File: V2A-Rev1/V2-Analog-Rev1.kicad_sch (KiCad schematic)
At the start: 39 parts, among them J1 Apple II, J2 DB15_Female_HighDensity_Mount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, J3 NOPAL, J4 NOWIFI, J5 VGA, J6 VGA, U1 SN74LVC8T245DGVR, U2 SN74LVC8T245DGVR, U3 SN74LVC8T245DGVR, U4 SN74LVC8T245DGVR, U5 PALCE16V8H-5JC/5, U6 Pi PICO W, U7 AZ1117I-H-3.3

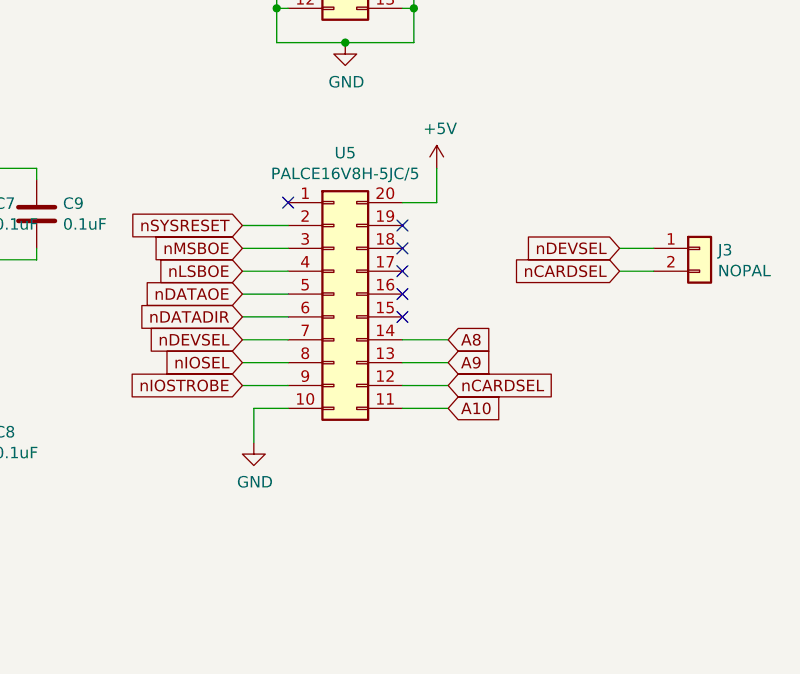
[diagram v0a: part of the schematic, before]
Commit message: Update design to use a PLCC socket for PAL/GAL.
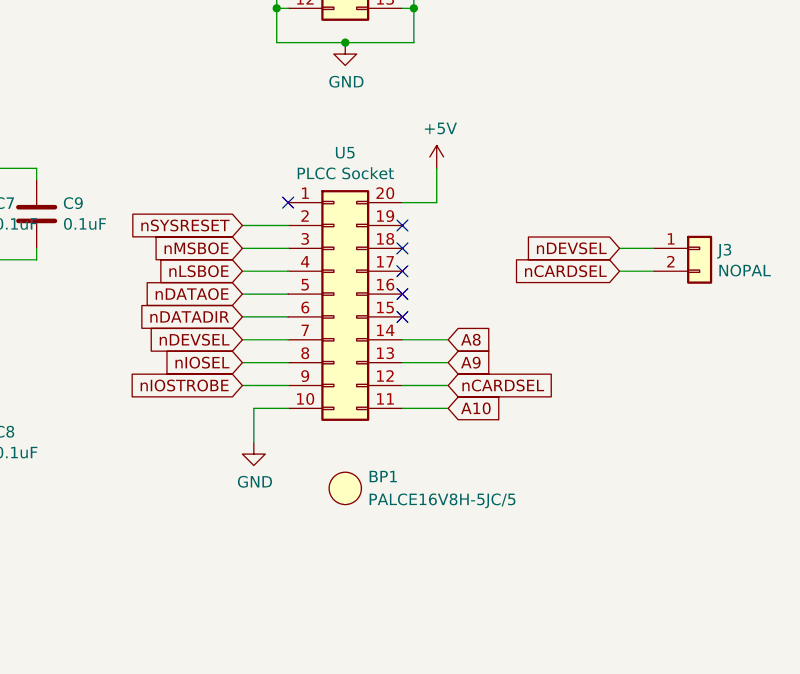
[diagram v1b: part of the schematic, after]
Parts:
- added BP1: PALCE16V8H-5JC/5, V2-Analog-Rev1:BOM_Placeholder, symbol V2-Analog-Rev1:BOM_Placeholder
- U5: value PALCE16V8H-5JC/5 -> PLCC Socket; footprint Package_LCC:PLCC-20 -> Package_LCC:PLCC-20_SMD-Socket; Digi-Key_PN 2156-PALCE16V8H-5JC/5-ND -> AE11102-ND; LCSC C3292615 -> C7058802; MPN PALCE16V8H-5JC/5 -> A-CCS 020-Z-SM; Manufacturer Lattice Semiconductor Corporation -> Assmann WSW Components
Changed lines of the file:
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@@
     (in_bom yes) (on_board yes)
     (property "Reference" "U5" (id 0) (at 234.95 121.4882 0))
-    (property "Value" "PALCE16V8H-5JC/5" (id 1) (at 234.95 123.7996 0))
-    (property "Footprint" "Package_LCC:PLCC-20" (id 2) (at 233.68 137.16 0)
-      (effects (font (size 1.27 1.27)) hide)
-    )
-    (property "Datasheet" "https://rocelec.widen.net/view/pdf/pmuxehviwj/LATTS01075-1.pdf?t.download=true&u=5oefqw" (id 3) (at 233.68 137.16 0)
-      (effects (font (size 1.27 1.27)) hide)
-    )
-    (property "Description" "EE PLD, 5NS, PAL-TYPE" (id 4) (at 233.68 137.16 0)
-      (effects (font (size 1.27 1.27)) hide)
-    )
-    (property "Digi-Key_PN" "2156-PALCE16V8H-5JC/5-ND" (id 5) (at 233.68 137.16 0)
-      (effects (font (size 1.27 1.27)) hide)
-    )
-    (property "MPN" "PALCE16V8H-5JC/5" (id 6) (at 233.68 137.16 0)
-      (effects (font (size 1.27 1.27)) hide)
-    )
-    (property "Manufacturer" "Lattice Semiconductor Corporation" (id 7) (at 233.68 137.16 0)
-      (effects (font (size 1.27 1.27)) hide)
-    )
-    (property "LCSC" "C3292615" (id 8) (at 233.68 137.16 0)
+    (property "Value" "PLCC Socket" (id 1) (at 234.95 123.7996 0))
+    (property "Footprint" "Package_LCC:PLCC-20_SMD-Socket" (id 2) (at 233.68 137.16 0)
+      (effects (font (size 1.27 1.27)) hide)
+    )
+    (property "Datasheet" "http://www.assmann-wsw.com/uploads/datasheets/ASS_0142_CO.pdf" (id 3) (at 233.68 137.16 0)
+      (effects (font (size 1.27 1.27)) hide)
+    )
+    (property "Description" "CONN SOCKET PLCC 20POS TIN" (id 4) (at 233.68 137.16 0)
+      (effects (font (size 1.27 1.27)) hide)
+    )
+    (property "Digi-Key_PN" "AE11102-ND" (id 5) (at 233.68 137.16 0)
+      (effects (font (size 1.27 1.27)) hide)
+    )
+    (property "MPN" "A-CCS 020-Z-SM" (id 6) (at 233.68 137.16 0)
+      (effects (font (size 1.27 1.27)) hide)
+    )
+    (property "Manufacturer" "Assmann WSW Components" (id 7) (at 233.68 137.16 0)
+      (effects (font (size 1.27 1.27)) hide)
+    )
+    (property "LCSC" "C7058802" (id 8) (at 233.68 137.16 0)
       (effects (font (size 1.27 1.27)) hide)
     )
@@
     (pin "2")
   )
+  (symbol (lib_id "V2-Analog-Rev1:BOM_Placeholder") (at 234.95 158.75 0) (unit 1)
+    (in_bom yes) (on_board yes) (fields_autoplaced)
+    (property "Reference" "BP1" (id 0) (at 237.49 157.4799 0)
+      (effects (font (size 1.27 1.27)) (justify left))
+    )
+    (property "Value" "PALCE16V8H-5JC/5" (id 1) (at 237.49 160.0199 0)
+      (effects (font (size 1.27 1.27)) (justify left))
+    )
+    (property "Footprint" "V2-Analog-Rev1:BOM_Placeholder" (id 2) (at 234.95 158.75 0)
+      (effects (font (size 1.27 1.27)) hide)
+    )
+    (property "Datasheet" "~" (id 3) (at 234.95 158.75 0)
+      (effects (font (size 1.27 1.27)) hide)
+    )
+    (property "Description" "EE PLD, 5NS, PAL-TYPE" (id 4) (at 234.95 158.75 0)
+      (effects (font (size 1.27 1.27)) hide)
+    )
+    (property "Digi-Key_PN" "2156-PALCE16V8H-5JC/5-ND" (id 5) (at 234.95 158.75 0)
+      (effects (font (size 1.27 1.27)) hide)
+    )
+    (property "LCSC" "C3292615" (id 6) (at 234.95 158.75 0)
+      (effects (font (size 1.27 1.27)) hide)
+    )
+    (property "MPN" "PALCE16V8H-5JC/5" (id 7) (at 234.95 158.75 0)
+      (effects (font (size 1.27 1.27)) hide)
+    )
+    (property "Manufacturer" "Lattice Semiconductor Corporation" (id 8) (at 234.95 158.75 0)
+      (effects (font (size 1.27 1.27)) hide)
+    )
+  )
   (symbol (lib_id "Connector_Generic:Conn_02x08_Odd_Even") (at 140.97 163.83 180) (unit 1)
     (in_bom yes) (on_board yes) (fields_autoplaced)
@@
       (reference "#PWR0109") (unit 1) (value "GND") (footprint "")
     )
+    (path "/0fb6992d-b8f1-4eb5-800c-0c88afa8e4e5"
+      (reference "BP1") (unit 1) (value "PALCE16V8H-5JC/5") (footprint "V2-Analog-Rev1:BOM_Placeholder")
+    )
     (path "/00000000-0000-0000-0000-00006382c831"
       (reference "C1") (unit 1) (value "0.1uF") (footprint "Capacitor_SMD:C_0402_1005Metric_Pad0.74x0.62mm_HandSolder")
@@
     )
     (path "/00000000-0000-0000-0000-000066540aaf"
-      (reference "U5") (unit 1) (value "PALCE16V8H-5JC/5") (footprint "Package_LCC:PLCC-20")
+      (reference "U5") (unit 1) (value "PLCC Socket") (footprint "Package_LCC:PLCC-20_SMD-Socket")
     )
     (path "/00000000-0000-0000-0000-000063a68952"

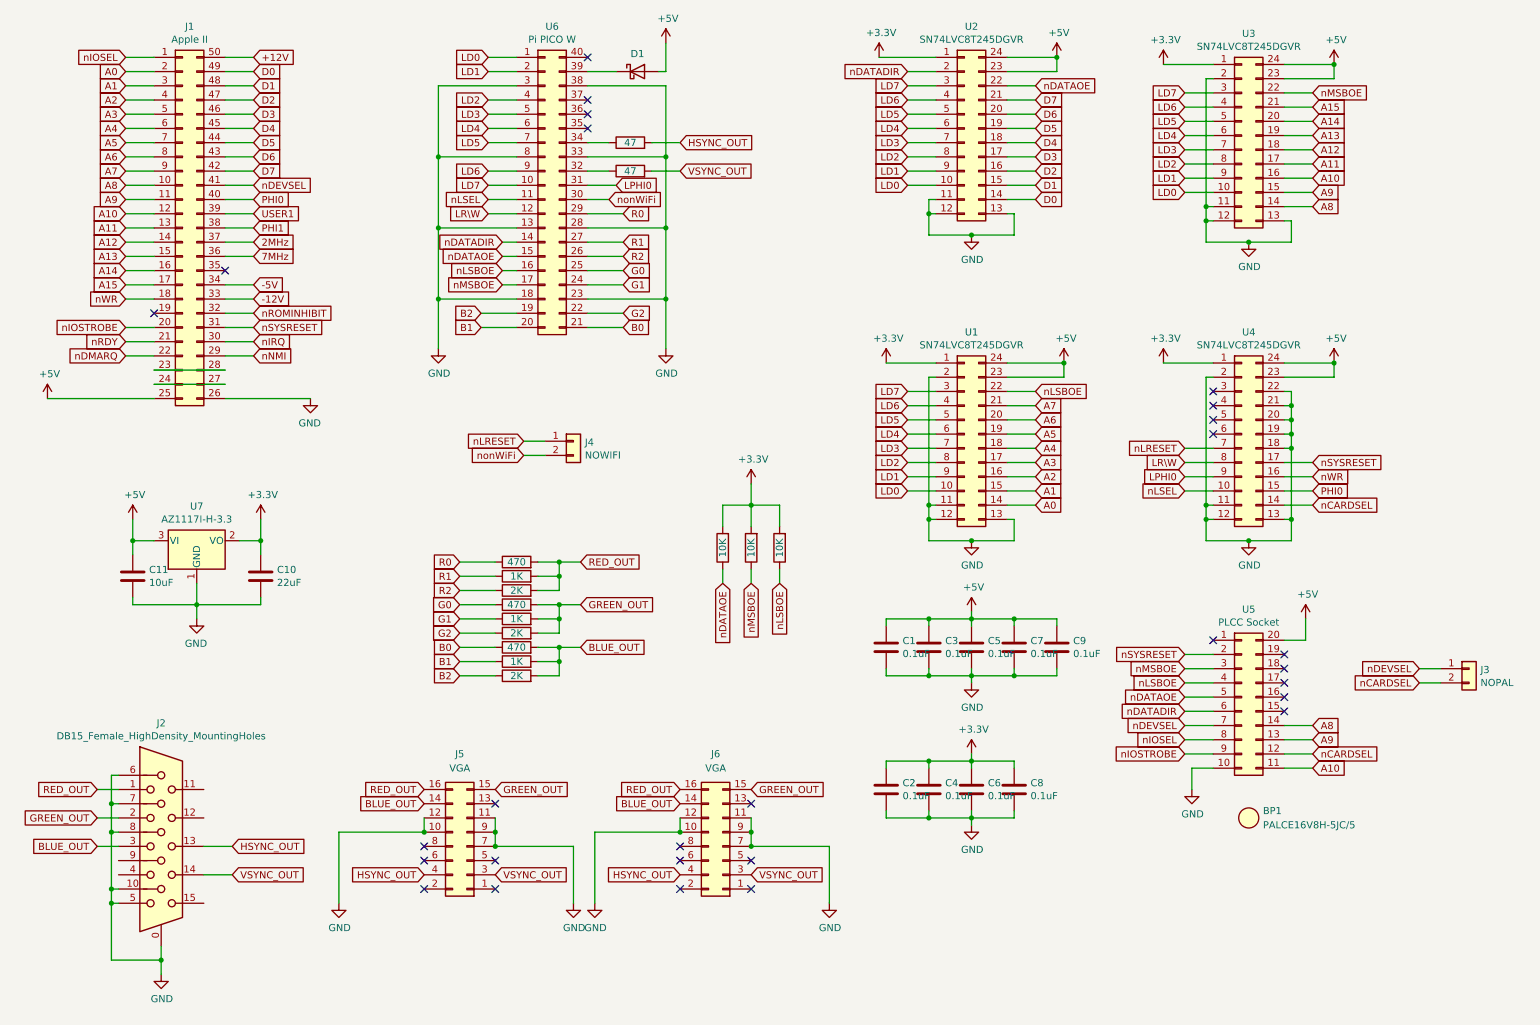
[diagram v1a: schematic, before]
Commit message: Added socket for PLCC. Reorganized layout for improved VGA picture clarity.
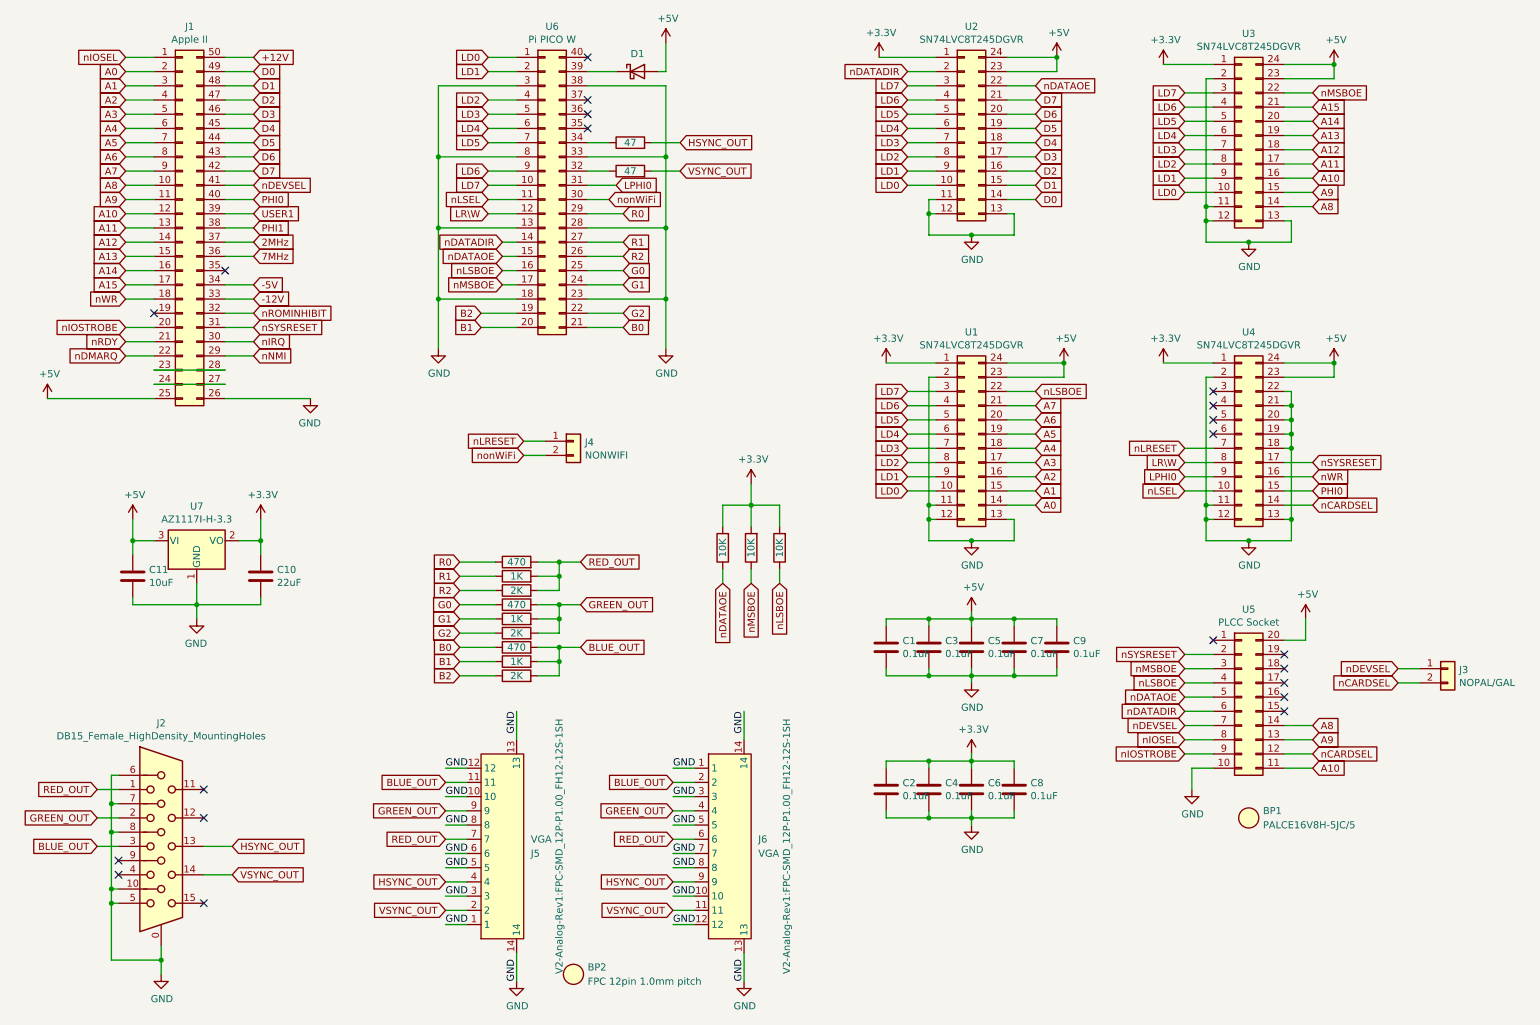
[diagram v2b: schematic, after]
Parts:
- added BP2: FPC 12pin 1.0mm pitch, V2-Analog-Rev1:BOM_Placeholder, symbol V2-Analog-Rev1:BOM_Placeholder
- BP1: Digi-Key_PN 2156-PALCE16V8H-5JC/5-ND -> (none); PN_DigiKey (none) -> 2156-PALCE16V8H-5JC/5-ND; PN_Mouser (none) -> Not Assigned
- C1, C2, C3, C4, C5, C6, C7, C8, C9: Digi-Key_PN 1276-6720-1-ND -> (none); PN_DigiKey (none) -> 1276-6720-1-ND; PN_Mouser (none) -> 187-CL05B104KA5NNNC
- C10: Digi-Key_PN 1276-CL21A226MAYNNNECT-ND -> (none); PN_DigiKey (none) -> 1276-CL21A226MAYNNNECT-ND; PN_Mouser (none) -> 187-CL21A226MAYNNNE
- C11: Digi-Key_PN 1276-2891-1-ND -> (none); PN_DigiKey (none) -> 1276-2891-1-ND; PN_Mouser (none) -> 187-CL21A106KAYNNNE
- D1: Digi-Key_PN 3372-SS14FTR-ND -> (none); PN_DigiKey (none) -> 3372-SS14FTR-ND; PN_Mouser (none) -> 833-SS14FL-TP
- J2: footprint Connector_Dsub:DSUB-15-HD_Female_Horizontal_P2.29x1.98mm_EdgePinOffset3.03mm_Housed_MountingHolesOffset4.94mm -> V2-Analog-Rev1:DSUB-15-HD_Female_Horizontal_P2.29x1.98mm_EdgePinOffset3.03mm_Housed_MountingHolesOffset4.94mm; symbol Connector:DB15_Female_HighDensity_MountingHoles -> V2-Analog-Rev1:DB15_Female_HighDensity_MountingHoles; Digi-Key_PN L77HDE15SD1CH4FVGA-ND -> (none); PN_DigiKey (none) -> L77HDE15SD1CH4FVGA-ND; PN_Mouser (none) -> 523-7HDE15SD1CH4FVGA
- J3: value NOPAL -> NOPAL/GAL
- J4: value NOWIFI -> NONWIFI
- J5, J6: footprint Connector_PinHeader_2.54mm:PinHeader_2x08_P2.54mm_Vertical -> V2-Analog-Rev1:FPC-SMD_12P-P1.00_FH12-12S-1SH; symbol Connector_Generic:Conn_02x08_Odd_Even -> V2-Analog-Rev1:FH12-12S-1SH(55); Digi-Key_PN SAM1058-08-ND -> (none); LCSC C706898 -> C5148307; MPN TSW-108-14-T-D -> FH12-12S-1SH(55); Manufacturer Samtec Inc. -> Hirose Electric Co Ltd; PN_DigiKey (none) -> H124709CT-ND; PN_Mouser (none) -> 798-FH1212S1SH55
- R1, R4, R7: Digi-Key_PN P470LCT-ND -> (none); PN_DigiKey (none) -> P470LCT-ND; PN_Mouser (none) -> 667-ERJ-2RKF4700X
- R10, R11: Digi-Key_PN P47.0LCT-ND -> (none); PN_DigiKey (none) -> P47.0LCT-ND; PN_Mouser (none) -> 667-ERJ-2RKF47R0X
- R12, R13, R14: Digi-Key_PN P10.0KHCT-ND -> (none); PN_DigiKey (none) -> P10.0KHCT-ND; PN_Mouser (none) -> 667-ERJ-3EKF1002V
- R2, R5, R8: Digi-Key_PN P1.00KLCT-ND -> (none); PN_DigiKey (none) -> P1.00KLCT-ND; PN_Mouser (none) -> 667-ERJ-2RKF1001X
- R3, R6, R9: Digi-Key_PN P2.00KLCT-ND -> (none); PN_DigiKey (none) -> P2.00KLCT-ND; PN_Mouser (none) -> 667-ERJ-2RKF2001X
- U1, U2, U3, U4: Digi-Key_PN 296-19287-1-ND -> (none); PN_DigiKey (none) -> 296-19287-1-ND; PN_Mouser (none) -> 595-SN74LVC8T245DGVR
- U5: footprint Package_LCC:PLCC-20_SMD-Socket -> V2-Analog-Rev1:A-CCS_020-Z-SM_SMD-Socket; Digi-Key_PN AE11102-ND -> (none); PN_DigiKey (none) -> AE11102-ND; PN_Mouser (none) -> 517-8420-21B1-RK-TR
- U6: Digi-Key_PN 2648-SC0918CT-ND -> (none); PN_DigiKey (none) -> 2648-SC0918CT-ND; PN_Mouser (none) -> 358-SC0918
- U7: Digi-Key_PN 31-AZ1117H-3.3TRG1CT-ND -> (none); PN_DigiKey (none) -> 31-AZ1117H-3.3TRG1CT-ND; PN_Mouser (none) -> 621-AZ1117H-3.3TRG1
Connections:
- net BLUE_OUT: now also J5.11, J6.2; no longer J5.14 (Pin_14), J6.14 (Pin_14)
- net GND: now also J5.1, J5.13, J5.14, J5.3, J5.5, J5.6, J5.8, J6.1, J6.13, J6.14, J6.3, J6.5, J6.8; no longer J5.11 (Pin_11), J5.7 (Pin_7), J5.9 (Pin_9), J6.11 (Pin_11), J6.9 (Pin_9)
- net GREEN_OUT: now also J5.9, J6.4; no longer J5.15 (Pin_15), J6.15 (Pin_15)
- net HSYNC_OUT: now also J6.9; no longer J6.4 (Pin_4)
- net RED_OUT: now also J5.7, J6.6; no longer J5.16 (Pin_16), J6.16 (Pin_16)
- net VSYNC_OUT: now also J5.2, J6.11; no longer J5.3 (Pin_3), J6.3 (Pin_3)
- no-connect marks 28 -> 21
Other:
- moved on the sheet: J3

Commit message: Added Left and Right Fiducial break away Rails
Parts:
- BP1: PN_Mouser Not Assigned -> Unavailable
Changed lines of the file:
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@@
       (effects (font (size 1.27 1.27)) hide)
     )
-    (property "PN_Mouser" "Not Assigned" (id 9) (at 234.95 158.75 0)
+    (property "PN_Mouser" "Unavailable" (id 9) (at 234.95 158.75 0)
       (effects (font (size 1.27 1.27)) hide)
     )
